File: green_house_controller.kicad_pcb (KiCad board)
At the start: 2 copper layers, 101.6 x 76.2 mm, 105 parts, among them J1 TC2030-IDC, J2 Screw_Terminal_01x05, J3 USB_B_Mini, J4 Screw_Terminal_01x06, Q1 2N7002, Q10 DMG3406L, Q11 DMP3068L, Q12 DMG3406L, Q13 2N7002, Q14 DMP3068L, Q15 DMG3406L, Q16 DMP3068L, Q17 DMG3406L, Q19 2N7002, Q2 2N7002, Q3 DMP3068L, Q4 DMG3406L, Q5 DMP3068L, Q6 DMG3406L, Q7 2N7002, Q8 2N7002, Q9 DMP3068L, U1 ESP32-WROVER, U2 TPS54231, U3 TLP3546, U4 TLP3546, U5 TLP3546, U6 TLP3546, U7 LM2733XMF

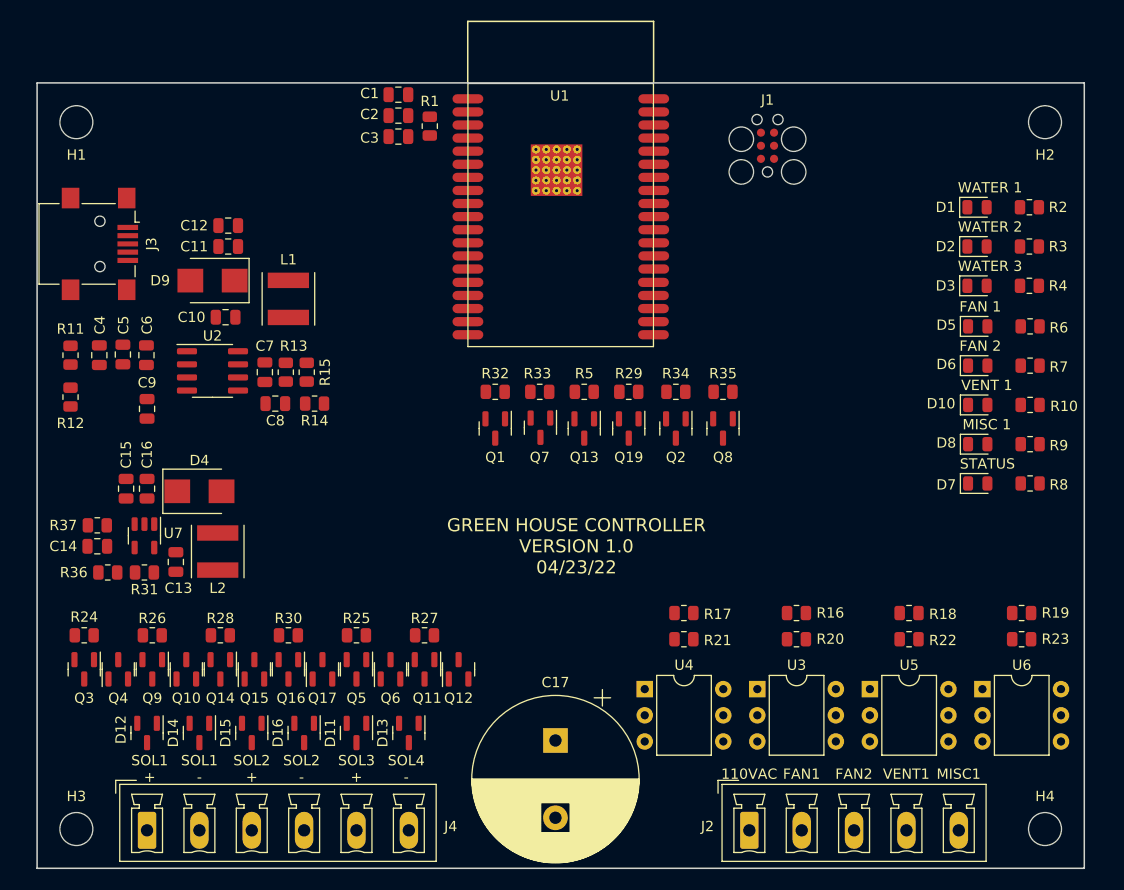
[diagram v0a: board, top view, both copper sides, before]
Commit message: Added connector for temperature sensor. Started to route board.
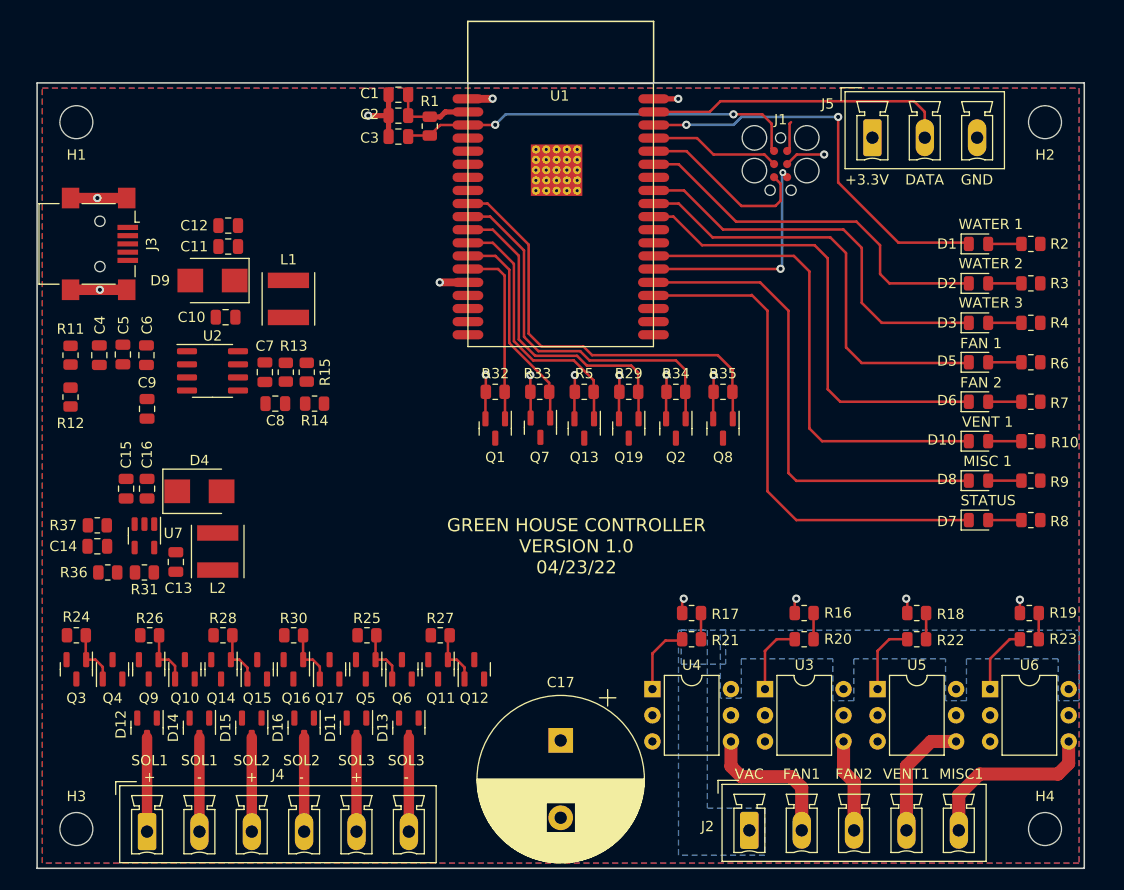
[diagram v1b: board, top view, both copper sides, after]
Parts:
- added J5: Screw_Terminal_01x03, Connector_Phoenix_MC_HighVoltage:PhoenixContact_MCV_1,5_3-G-5.08_1x03_P5.08mm_Vertical, F.Cu at (181.1, 63.1)
- moved D3 3.60 mm to (191.4, 81.1)
- moved R4 3.60 mm to (196.5, 81.1)
- moved D2 3.58 mm to (191.4, 77.2)
- moved R3 3.58 mm to (196.5, 77.2)
- moved D1 3.56 mm to (191.4, 73.4)
- moved R2 3.56 mm to (196.5, 73.4)
- moved D7 3.56 mm to (191.4, 100.2)
- moved R8 3.56 mm to (196.5, 100.2)
- moved D8 3.54 mm to (191.4, 96.4)
- moved R9 3.54 mm to (196.5, 96.4)
- moved D10 3.52 mm to (191.4, 92.5)
- moved R10 3.52 mm to (196.5, 92.5)
- moved D6 3.50 mm to (191.4, 88.7)
- moved R7 3.50 mm to (196.5, 88.7)
- moved D5 3.48 mm to (191.4, 84.9)
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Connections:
- C11 pad 1: +3.3V -> +3V3
- C12 pad 1: +3.3V -> +3V3
- J1 pad 2: /microcontroller/+3.3V -> +3V3
- L1 pad 2: +3.3V -> +3V3
- R14 pad 1: +3.3V -> +3V3
- U1 pad 10: unconnected-(U1-Pad10) -> /microcontroller/SOL_3_CLOSE_CTRL
- U1 pad 11: /microcontroller/MISC_1_CTRL -> /microcontroller/SOL_2_OPEN_CTRL
- U1 pad 12: /microcontroller/VENT_1_CTRL -> /microcontroller/SOL_2_CLOSE_CTRL
- U1 pad 13: /microcontroller/FAN_2_CTRL -> /microcontroller/SOL_1_OPEN_CTRL
- U1 pad 14: /microcontroller/FAN_1_CTRL -> /microcontroller/SOL_1_CLOSE_CTRL
- U1 pad 4: /microcontroller/SOL_3_CLOSE_CTRL -> unconnected-(U1-Pad4)
- U1 pad 5: /microcontroller/SOL_3_OPEN_CTRL -> /microcontroller/MISC_1_CTRL
- U1 pad 6: /microcontroller/SOL_2_CLOSE_CTRL -> /microcontroller/VENT_1_CTRL
- U1 pad 7: /microcontroller/SOL_2_OPEN_CTRL -> /microcontroller/FAN_2_CTRL
- U1 pad 8: /microcontroller/SOL_1_CLOSE_CTRL -> /microcontroller/FAN_1_CTRL
- U1 pad 9: /microcontroller/SOL_1_OPEN_CTRL -> /microcontroller/SOL_3_OPEN_CTRL
- U3 pad 6: unconnected-(U3-Pad6) -> /relay control/110VAC
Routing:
- net GND: track 0.00 -> 61.5 mm, vias 0 -> 17
- net /microcontroller/LED_STATUS: track 0.00 -> 49.9 mm
- net /microcontroller/LED_MISC_1: track 0.00 -> 47.8 mm
- net /microcontroller/LED_VENT_1: track 0.00 -> 46.9 mm
- net /microcontroller/LED_FAN_2: track 0.00 -> 45.4 mm
- net /microcontroller/LED_FAN_1: track 0.00 -> 42.4 mm
- net /microcontroller/SOL_3_OPEN_CTRL: track 0.00 -> 42.2 mm
- net /microcontroller/LED_SOL_1: track 0.00 -> 39.7 mm, vias 0 -> 2
- net /microcontroller/RESET: track 0.00 -> 39.3 mm, vias 0 -> 2
- net /microcontroller/LED_SOL_3: track 0.00 -> 39.0 mm
- net /microcontroller/LED_SOL_2: track 0.00 -> 37.0 mm
- net /microcontroller/SOL_3_CLOSE_CTRL: track 0.00 -> 36.9 mm
- net /microcontroller/SOL_2_OPEN_CTRL: track 0.00 -> 31.5 mm
- net /microcontroller/DHT11_DATA: track 0.00 -> 29.7 mm
- net /microcontroller/SOL_2_CLOSE_CTRL: track 0.00 -> 25.9 mm
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- added copper zone on F.Cu, net +3V3
- added copper zone on B.Cu, net /relay control/110VAC
- added copper zone on B.Cu, net GND
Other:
- board text added: "+3.3V"
- board text added: "DATA"
- board text added: "GND"
- board text added: "SOL3 -"
- board text added: "VAC"
- board text removed: "110VAC"
- board text removed: "SOL4 -"

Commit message: Added clamping diode for 24V net.
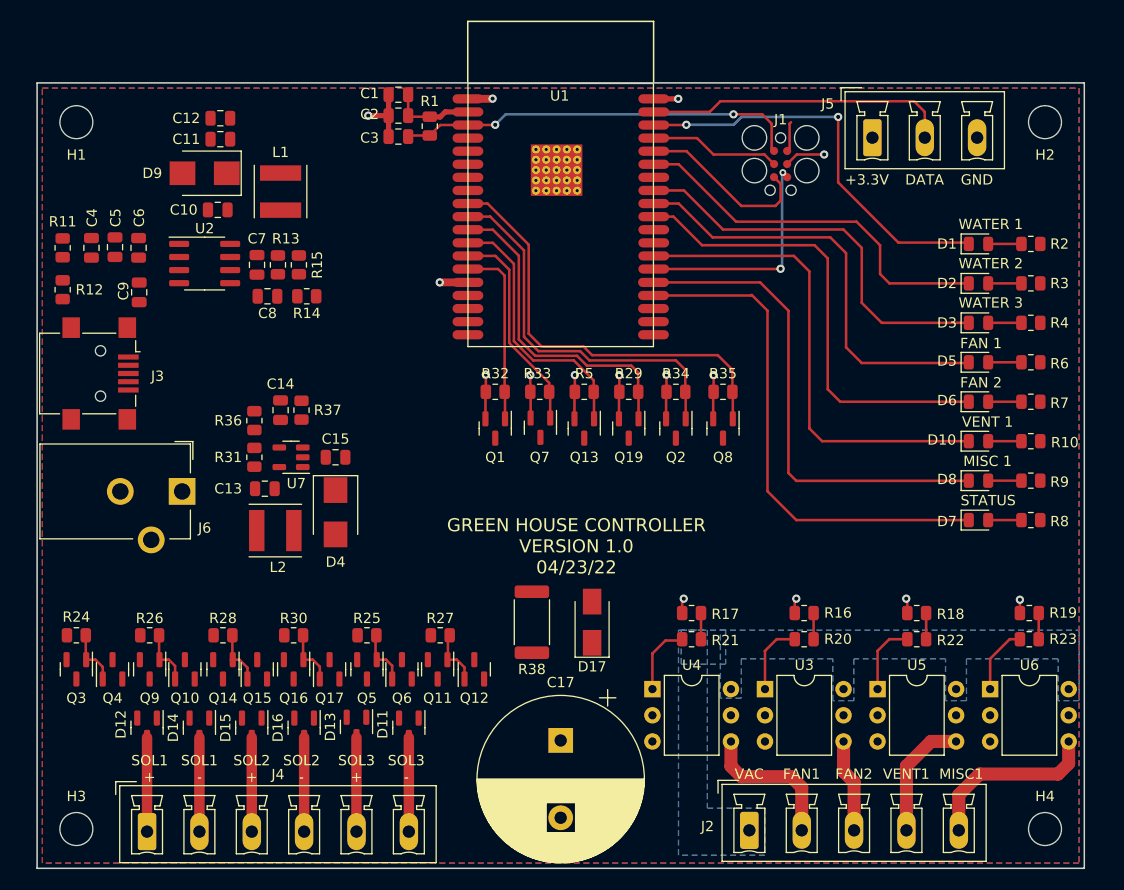
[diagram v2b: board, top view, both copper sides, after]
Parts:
- removed C16: 2200uF, Capacitor_SMD:C_0805_2012Metric
- added D17: B140-E3, Diode_SMD:D_SMA, F.Cu at (153.9, 110.1)
- added J6: Barrel_Jack, Connector_BarrelJack:BarrelJack_CUI_PJ-102AH_Horizontal, F.Cu at (114.2, 97.4)
- added R38: 100, Resistor_SMD:R_2512_6332Metric, F.Cu at (148.1, 110.1)
- R24, R25, R26, R27, R28, R29, R30, R32, R33, R34, R35, R5: value R_US -> 1K
- R36, R37: value ?K -> 1K
- moved R37 22.7 mm to (125.7, 89.5), turned to 90 degrees
- moved C14 22.1 mm to (123.7, 89.5), turned to 90 degrees
- moved C15 20.5 mm to (129.0, 94.1), turned to 180 degrees
- moved R36 20.5 mm to (121.2, 90.6), turned to 90 degrees
- moved U7 16.1 mm to (124.7, 94.1), turned to 180 degrees
- moved R31 15.5 mm to (121.2, 94.1), turned to 90 degrees
- moved D4 13.4 mm to (129.0, 99.4), turned to -90 degrees
- moved J3 12.6 mm to (106.2, 86.0)
- moved C9 11.3 mm to (110.0, 78.1)
- moved C13 11.2 mm to (122.2, 97.2), turned to 0 degrees
- moved C10 10.4 mm to (117.6, 70.1)
- moved C12 10.4 mm to (117.9, 61.2)
- moved C5 10.4 mm to (107.6, 73.7)
- moved C7 10.4 mm to (121.4, 75.4)
- moved C8 10.4 mm to (122.4, 78.5)
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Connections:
- C17 pad 1: +24V -> +VDC
- D11 pad 2: +24V -> +VDC
- D12 pad 2: +24V -> +VDC
- D13 pad 2: +24V -> +VDC
- D14 pad 2: +24V -> +VDC
- D15 pad 2: +24V -> +VDC
- D16 pad 2: +24V -> +VDC
- Q11 pad 3: +24V -> +VDC
- Q14 pad 3: +24V -> +VDC
- Q16 pad 3: +24V -> +VDC
- Q3 pad 3: +24V -> +VDC
- Q5 pad 3: +24V -> +VDC
- Q9 pad 3: +24V -> +VDC
- R24 pad 1: +24V -> +VDC
- R25 pad 1: +24V -> +VDC
- R26 pad 1: +24V -> +VDC
- R27 pad 1: +24V -> +VDC
- R28 pad 1: +24V -> +VDC
- R30 pad 1: +24V -> +VDC
- U3 pad 6: /relay control/110VAC -> unconnected-(U3-Pad6)
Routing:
- net GND: track 61.5 -> 50.6 mm, vias 17 -> 15

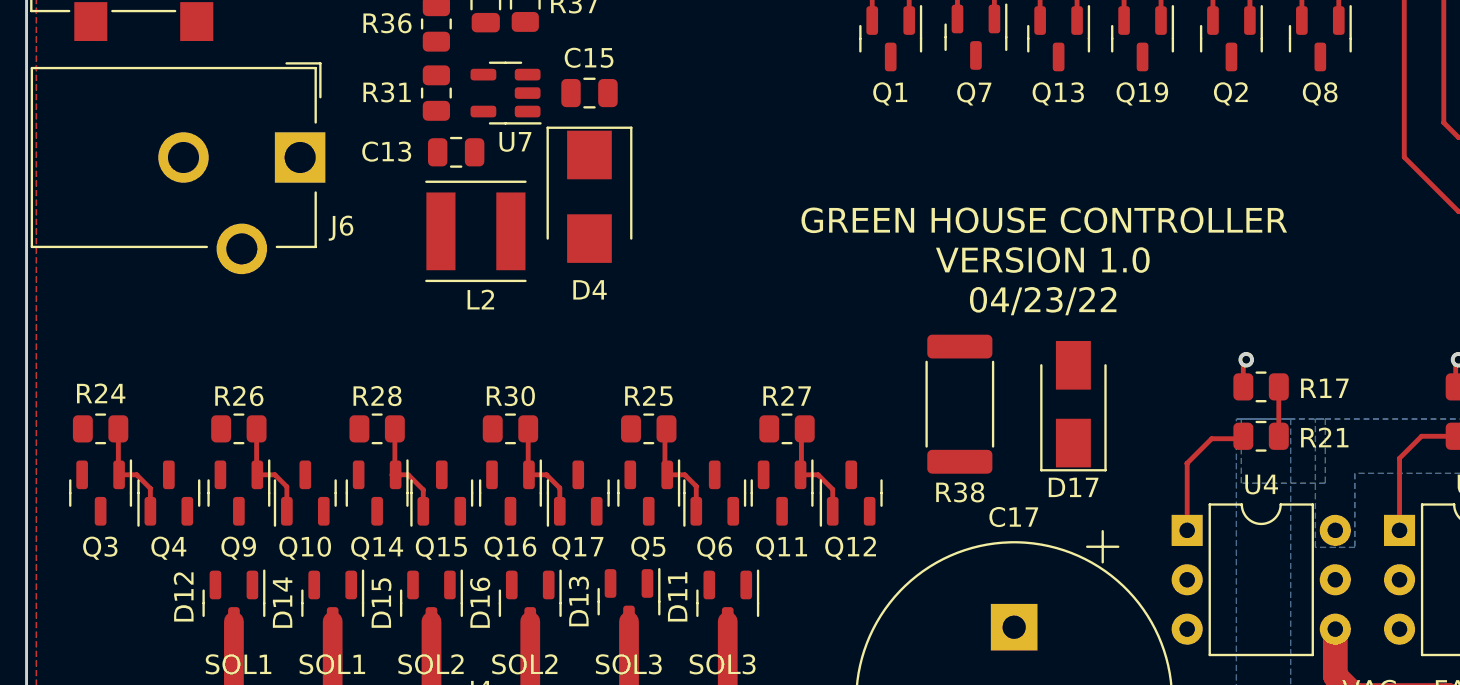
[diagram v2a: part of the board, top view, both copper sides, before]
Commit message: Flipped top fets for solenoid controls so that the body diode was pointing the correction direction.
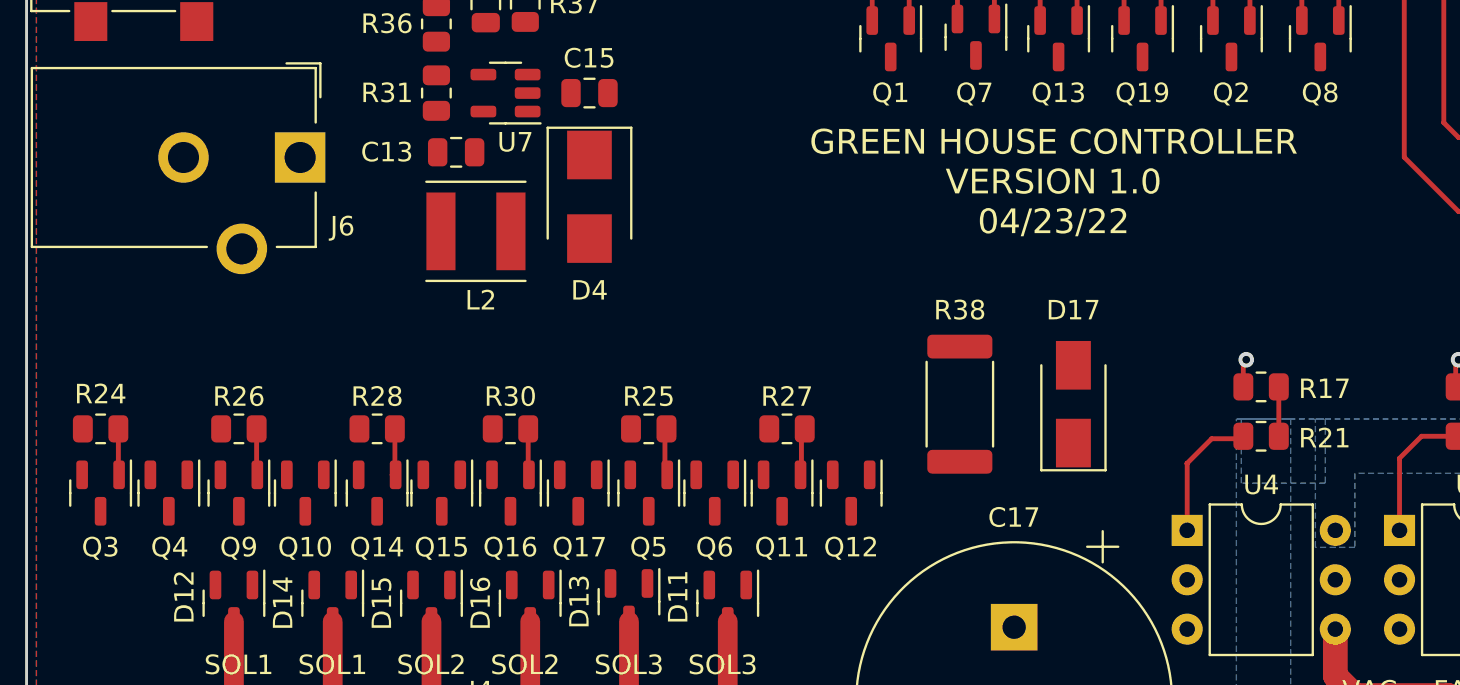
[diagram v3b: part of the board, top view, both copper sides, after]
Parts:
- turned Q10 to -90 degrees
- turned Q12 to -90 degrees
- turned Q15 to -90 degrees
- turned Q17 to -90 degrees
- turned Q4 to -90 degrees
- turned Q6 to -90 degrees
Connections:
- Q11 pad 2: /solenoid control/SOL_3_PWR- -> +VDC
- Q11 pad 3: +VDC -> /solenoid control/SOL_3_PWR-
- Q14 pad 2: /solenoid control/SOL_2_PWR+ -> +VDC
- Q14 pad 3: +VDC -> /solenoid control/SOL_2_PWR+
- Q16 pad 2: /solenoid control/SOL_2_PWR- -> +VDC
- Q16 pad 3: +VDC -> /solenoid control/SOL_2_PWR-
- Q3 pad 2: /solenoid control/SOL_1_PWR+ -> +VDC
- Q3 pad 3: +VDC -> /solenoid control/SOL_1_PWR+
- Q5 pad 2: /solenoid control/SOL_3_PWR+ -> +VDC
- Q5 pad 3: +VDC -> /solenoid control/SOL_3_PWR+
- Q9 pad 2: /solenoid control/SOL_1_PWR- -> +VDC
- Q9 pad 3: +VDC -> /solenoid control/SOL_1_PWR-
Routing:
- net Net-(Q2-Pad3): track 5.54 -> 2.40 mm
- net Net-(Q7-Pad3): track 5.51 -> 2.39 mm
- net Net-(Q17-Pad1): track 5.46 -> 2.37 mm
- net Net-(Q1-Pad3): track 5.45 -> 2.38 mm
- net Net-(Q12-Pad1): track 5.48 -> 2.44 mm
- net Net-(Q13-Pad3): track 5.46 -> 2.43 mm

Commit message: Continued with layout.
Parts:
- added SW1: SW_Push, Button_Switch_SMD:SW_SPST_B3S-1000, F.Cu at (132.1, 67.9)
- J2: value Screw_Terminal_01x05 -> Screw_Terminal_01x10; footprint Connector_Phoenix_MC_HighVoltage:PhoenixContact_MCV_1,5_5-G-5.08_1x05_P5.08mm_Vertical -> Connector_Phoenix_MC_HighVoltage:PhoenixContact_MCV_1,5_10-G-5.08_1x10_P5.08mm_Vertical
- U3, U4, U5, U6: value TLP3546 -> TLP3825TP1_F; footprint Package_DIP:DIP-6_W7.62mm -> Package_DIP:DIP-8_W7.62mm
- moved D17 31.5 mm to (122.7, 106.3), turned to 180 degrees
- moved J2 22.1 mm to (147.1, 130.5)
- moved R38 19.6 mm to (133.6, 96.9)
- moved C17 14.5 mm to (142.7, 109.6), turned to 90 degrees
- moved U6 12.7 mm to (180.1, 114.3)
- moved U5 11.9 mm to (169.9, 114.3)
- moved U3 11.2 mm to (159.8, 114.3)
- moved U4 10.4 mm to (149.6, 114.3)
- moved R19 9.77 mm to (186.9, 106.6)
- moved R23 9.77 mm to (186.9, 109.1)
- moved R16 9.77 mm to (165.1, 106.6)
- moved R17 9.77 mm to (154.2, 106.6)
- moved R18 9.77 mm to (176.0, 106.6)
- moved R20 9.77 mm to (165.1, 109.1)
- moved R21 9.77 mm to (154.2, 109.1)
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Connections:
- J2 pad 2: /relay control/FAN_1_PWR -> Earth
- J2 pad 3: /relay control/FAN_2_PWR -> /relay control/FAN_1_PWR
- J2 pad 4: /relay control/VENT_1_PWR -> Earth
- J2 pad 5: /relay control/MISC_1_PWR -> /relay control/FAN_2_PWR
- U3 pad 1: Net-(R20-Pad1) -> unconnected-(U3-Pad1)
- U3 pad 2: GND -> Net-(R20-Pad1)
- U3 pad 3: unconnected-(U3-Pad3) -> GND
- U3 pad 4: /relay control/FAN_2_PWR -> unconnected-(U3-Pad4)
- U3 pad 5: unconnected-(U3-Pad5) -> /relay control/FAN_2_PWR
- U4 pad 1: Net-(R21-Pad1) -> unconnected-(U4-Pad1)
- U4 pad 2: GND -> Net-(R21-Pad1)
- U4 pad 3: unconnected-(U4-Pad3) -> GND
- U4 pad 4: /relay control/FAN_1_PWR -> unconnected-(U4-Pad4)
- U4 pad 5: unconnected-(U4-Pad5) -> /relay control/FAN_1_PWR
- U4 pad 6: /relay control/110VAC -> unconnected-(U4-Pad6)
- U5 pad 1: Net-(R22-Pad1) -> unconnected-(U5-Pad1)
- U5 pad 2: GND -> Net-(R22-Pad1)
- U5 pad 3: unconnected-(U5-Pad3) -> GND
- U5 pad 4: /relay control/VENT_1_PWR -> unconnected-(U5-Pad4)
- U5 pad 5: unconnected-(U5-Pad5) -> /relay control/VENT_1_PWR
- U5 pad 6: /relay control/110VAC -> unconnected-(U5-Pad6)
- U6 pad 1: Net-(R23-Pad1) -> unconnected-(U6-Pad1)
- U6 pad 2: GND -> Net-(R23-Pad1)
- U6 pad 3: unconnected-(U6-Pad3) -> GND
- U6 pad 4: /relay control/MISC_1_PWR -> unconnected-(U6-Pad4)
- U6 pad 5: unconnected-(U6-Pad5) -> /relay control/MISC_1_PWR
- U6 pad 6: /relay control/110VAC -> unconnected-(U6-Pad6)
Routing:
- net +VDC: track 0.00 -> 129.4 mm
- net /microcontroller/MISC_1_CTRL: track 2.54 -> 84.0 mm, vias 0 -> 2
- net /microcontroller/VENT_1_CTRL: track 2.54 -> 72.1 mm, vias 0 -> 2
- net Net-(Q1-Pad3): track 2.38 -> 63.2 mm, vias 0 -> 2
- net Net-(Q7-Pad3): track 2.39 -> 58.0 mm, vias 0 -> 2
- net /microcontroller/FAN_2_CTRL: track 2.54 -> 58.0 mm, vias 0 -> 2
- net Net-(Q13-Pad3): track 2.43 -> 54.2 mm, vias 0 -> 2
- net Net-(Q17-Pad1): track 2.37 -> 53.2 mm, vias 0 -> 2
- net Net-(Q2-Pad3): track 2.40 -> 52.2 mm, vias 0 -> 2
- net Net-(Q12-Pad1): track 2.44 -> 51.2 mm
- net /microcontroller/FAN_1_CTRL: track 2.54 -> 51.0 mm, vias 0 -> 2
- net GND: track 50.6 -> 92.1 mm, vias 15 -> 31
- net /solenoid control/SOL_2_PWR-: track 9.14 -> 21.3 mm
- net /solenoid control/SOL_1_PWR+: track 9.14 -> 20.8 mm
- net /solenoid control/SOL_3_PWR+: track 9.14 -> 20.6 mm
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- added copper zone on B.Cu, net Earth
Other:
- board text added: "-"

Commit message: Finished layout for +24V regulator circuit.
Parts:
- added REF**: KiCad-Logo2_6mm_SilkScreen, Symbol:KiCad-Logo2_6mm_SilkScreen, F.Cu at (196.1, 115.1)
- moved C1 4.07 mm to (135.3, 63.0)
- moved C3 3.97 mm to (138.2, 65.5), turned to -90 degrees
- moved H3 1.53 mm to (102.4, 130.0)
- moved H1 1.52 mm to (102.4, 61.6)
- moved J3 1.52 mm to (104.7, 89.5)
- moved J6 1.52 mm to (112.6, 100.5)
- moved C13 1.40 mm to (123.6, 97.2)
- moved R38 0.10 mm to (133.6, 97.0)
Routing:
- net GND: track 92.1 -> 140.1 mm, vias 31 -> 39
- net /microcontroller/EN_24V: track 0.00 -> 39.7 mm
- net Net-(C14-Pad1): track 0.00 -> 4.81 mm
- net Net-(Q17-Pad1): track 53.2 -> 56.8 mm, vias 2 -> 4
- net /microcontroller/MISC_1_CTRL: track 84.0 -> 82.6 mm
- net /microcontroller/VENT_1_CTRL: track 72.1 -> 71.0 mm
- net /microcontroller/LED_SOL_1: track 39.7 -> 38.8 mm
- net +VDC: track 129.4 -> 128.6 mm
- net /microcontroller/RESET: track 49.9 -> 49.4 mm
- net Net-(D4-Pad2): track 0.00 -> 0.53 mm
- added copper zone on F.Cu, net +24V
- added copper zone on F.Cu, net /power supply/VIN
- added copper zone on F.Cu, net GND
- added copper zone on F.Cu, net Net-(C14-Pad1)
- added copper zone on F.Cu, net Net-(D4-Pad2)
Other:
- board size 101.6 x 76.2 mm -> 103.1 x 76.2 mm
- board text added: "Michael Bester"
